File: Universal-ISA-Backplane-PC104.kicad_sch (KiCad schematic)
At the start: 2 parts, among them J201 PC104, J202 PC104_16

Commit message: Initial steps for PCB layout
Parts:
- P201: renamed from J202; value PC104_16 -> (none); footprint Connector_PinSocket_2.54mm:PinSocket_2x20_P2.54mm_Vertical -> (none); symbol Connector_Generic:Conn_02x20_Row_Letter_First -> Universal-ISA-Backplane-symbols:PC104-Platform
- P201: renamed from J201; value PC104 -> (none); footprint Universal-ISA-Backplane:PC104_Platform -> (none); symbol Connector_Generic:Conn_02x32_Row_Letter_First -> Universal-ISA-Backplane-symbols:PC104-Platform
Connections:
- net +12V: now also P201.B9 (Pin_B9); no longer P201.b9 (Pin_b9)
- net +5V: now also P201.B29 (Pin_B29), P201.B3 (Pin_B3), P201.D16 (Pin_D16); no longer P201.b29 (Pin_b29), P201.b3 (Pin_b3), P201.d16 (Pin_d16)
- net -12V: now also P201.B7 (Pin_B7); no longer P201.b7 (Pin_b7)
- net -5V: now also P201.B5 (Pin_B5); no longer P201.b5 (Pin_b5)
- net AEN: now also P201.A11 (Pin_A11); no longer P201.a11 (Pin_a11)
- net BALE: now also P201.B28 (Pin_B28); no longer P201.b28 (Pin_b28)
- net BCLK: now also P201.B20 (Pin_B20); no longer P201.b20 (Pin_b20)
- net DRQ0: now also P201.D9 (Pin_D9); no longer P201.d9 (Pin_d9)
- net DRQ1: now also P201.B18 (Pin_B18); no longer P201.b18 (Pin_b18)
- net DRQ2: now also P201.B6 (Pin_B6); no longer P201.b6 (Pin_b6)
- net DRQ3: now also P201.B16 (Pin_B16); no longer P201.b16 (Pin_b16)
- net DRQ5: now also P201.D11 (Pin_D11); no longer P201.d11 (Pin_d11)
- net DRQ6: now also P201.D13 (Pin_D13); no longer P201.d13 (Pin_d13)
- net DRQ7: now also P201.D15 (Pin_D15); no longer P201.d15 (Pin_d15)
- net GND: now also P201.A32 (Pin_A32), P201.B1 (Pin_B1), P201.B31 (Pin_B31), P201.B32 (Pin_B32), P201.C0 (Pin_C0), P201.D0 (Pin_D0), P201.D18 (Pin_D18), P201.D19 (Pin_D19); no longer P201.a32 (Pin_a32), P201.b1 (Pin_b1), P201.b31 (Pin_b31), P201.b32 (Pin_b32), P201.c0 (Pin_c0), P201.d0 (Pin_d0), P201.d18 (Pin_d18), P201.d19 (Pin_d19)
- net IOCHRDY: now also P201.A10 (Pin_A10); no longer P201.a10 (Pin_a10)
- net IRQ10: now also P201.D3 (Pin_D3); no longer P201.d3 (Pin_d3)
- net IRQ11: now also P201.D4 (Pin_D4); no longer P201.d4 (Pin_d4)
- net IRQ12: now also P201.D5 (Pin_D5); no longer P201.d5 (Pin_d5)
- net IRQ14: now also P201.D7 (Pin_D7); no longer P201.d7 (Pin_d7)
- net IRQ15: now also P201.D6 (Pin_D6); no longer P201.d6 (Pin_d6)
- net IRQ3: now also P201.B25 (Pin_B25); no longer P201.b25 (Pin_b25)
- net IRQ4: now also P201.B24 (Pin_B24); no longer P201.b24 (Pin_b24)
- net IRQ5: now also P201.B23 (Pin_B23); no longer P201.b23 (Pin_b23)
- net IRQ6: now also P201.B22 (Pin_B22); no longer P201.b22 (Pin_b22)
- net IRQ7: now also P201.B21 (Pin_B21); no longer P201.b21 (Pin_b21)
- net IRQ9: now also P201.B4 (Pin_B4); no longer P201.b4 (Pin_b4)
- net LA17: now also P201.C8 (Pin_C8); no longer P201.c8 (Pin_c8)
- net LA18: now also P201.C7 (Pin_C7); no longer P201.c7 (Pin_c7)
- net LA19: now also P201.C6 (Pin_C6); no longer P201.c6 (Pin_c6)
- net LA20: now also P201.C5 (Pin_C5); no longer P201.c5 (Pin_c5)
- net LA21: now also P201.C4 (Pin_C4); no longer P201.c4 (Pin_c4)
- net LA22: now also P201.C3 (Pin_C3); no longer P201.c3 (Pin_c3)
- net LA23: now also P201.C2 (Pin_C2); no longer P201.c2 (Pin_c2)
- net OSC: now also P201.B30 (Pin_B30); no longer P201.b30 (Pin_b30)
- net RESET: now also P201.B2 (Pin_B2); no longer P201.b2 (Pin_b2)
- net SA0: now also P201.A31 (Pin_A31); no longer P201.a31 (Pin_a31)
- net SA1: now also P201.A30 (Pin_A30); no longer P201.a30 (Pin_a30)
- net SA10: now also P201.A21 (Pin_A21); no longer P201.a21 (Pin_a21)
- net SA11: now also P201.A20 (Pin_A20); no longer P201.a20 (Pin_a20)
- net SA12: now also P201.A19 (Pin_A19); no longer P201.a19 (Pin_a19)
- net SA13: now also P201.A18 (Pin_A18); no longer P201.a18 (Pin_a18)
- net SA14: now also P201.A17 (Pin_A17); no longer P201.a17 (Pin_a17)
- net SA15: now also P201.A16 (Pin_A16); no longer P201.a16 (Pin_a16)
- net SA16: now also P201.A15 (Pin_A15); no longer P201.a15 (Pin_a15)
- net SA17: now also P201.A14 (Pin_A14); no longer P201.a14 (Pin_a14)
- net SA18: now also P201.A13 (Pin_A13); no longer P201.a13 (Pin_a13)
- net SA19: now also P201.A12 (Pin_A12); no longer P201.a12 (Pin_a12)
- net SA2: now also P201.A29 (Pin_A29); no longer P201.a29 (Pin_a29)
- net SA3: now also P201.A28 (Pin_A28); no longer P201.a28 (Pin_a28)
- net SA4: now also P201.A27 (Pin_A27); no longer P201.a27 (Pin_a27)
- net SA5: now also P201.A26 (Pin_A26); no longer P201.a26 (Pin_a26)
- net SA6: now also P201.A25 (Pin_A25); no longer P201.a25 (Pin_a25)
- net SA7: now also P201.A24 (Pin_A24); no longer P201.a24 (Pin_a24)
- net SA8: now also P201.A23 (Pin_A23); no longer P201.a23 (Pin_a23)
- net SA9: now also P201.A22 (Pin_A22); no longer P201.a22 (Pin_a22)
- net SD0: now also P201.A9 (Pin_A9); no longer P201.a9 (Pin_a9)
- net SD1: now also P201.A8 (Pin_A8); no longer P201.a8 (Pin_a8)
- net SD10: now also P201.C13 (Pin_C13); no longer P201.c13 (Pin_c13)
- net SD11: now also P201.C14 (Pin_C14); no longer P201.c14 (Pin_c14)
- net SD12: now also P201.C15 (Pin_C15); no longer P201.c15 (Pin_c15)
- net SD13: now also P201.C16 (Pin_C16); no longer P201.c16 (Pin_c16)
- net SD14: now also P201.C17 (Pin_C17); no longer P201.c17 (Pin_c17)
- net SD15: now also P201.C18 (Pin_C18); no longer P201.c18 (Pin_c18)
- net SD2: now also P201.A7 (Pin_A7); no longer P201.a7 (Pin_a7)
- net SD3: now also P201.A6 (Pin_A6); no longer P201.a6 (Pin_a6)
- net SD4: now also P201.A5 (Pin_A5); no longer P201.a5 (Pin_a5)
- net SD5: now also P201.A4 (Pin_A4); no longer P201.a4 (Pin_a4)
- net SD6: now also P201.A3 (Pin_A3); no longer P201.a3 (Pin_a3)
- net SD7: now also P201.A2 (Pin_A2); no longer P201.a2 (Pin_a2)
- net SD8: now also P201.C11 (Pin_C11); no longer P201.c11 (Pin_c11)
- net SD9: now also P201.C12 (Pin_C12); no longer P201.c12 (Pin_c12)
- net TC: now also P201.B27 (Pin_B27); no longer P201.b27 (Pin_b27)
- net ~{DACK0}: now also P201.D8 (Pin_D8); no longer P201.d8 (Pin_d8)
- net ~{DACK1}: now also P201.B17 (Pin_B17); no longer P201.b17 (Pin_b17)
- net ~{DACK2}: now also P201.B26 (Pin_B26); no longer P201.b26 (Pin_b26)
- net ~{DACK3}: now also P201.B15 (Pin_B15); no longer P201.b15 (Pin_b15)
- net ~{DACK5}: now also P201.D10 (Pin_D10); no longer P201.d10 (Pin_d10)
- net ~{DACK6}: now also P201.D12 (Pin_D12); no longer P201.d12 (Pin_d12)
- net ~{DACK7}: now also P201.D14 (Pin_D14); no longer P201.d14 (Pin_d14)
- net ~{IOCHK}: now also P201.A1 (Pin_A1); no longer P201.a1 (Pin_a1)
- net ~{IOCS16}: now also P201.D2 (Pin_D2); no longer P201.d2 (Pin_d2)
- net ~{IOR}: now also P201.B14 (Pin_B14); no longer P201.b14 (Pin_b14)
- net ~{IOW}: now also P201.B13 (Pin_B13); no longer P201.b13 (Pin_b13)
- net ~{MASTER}: now also P201.D17 (Pin_D17); no longer P201.d17 (Pin_d17)
- net ~{MEMCS16}: now also P201.D1 (Pin_D1); no longer P201.d1 (Pin_d1)
- net ~{MEMR}: now also P201.C9 (Pin_C9); no longer P201.c9 (Pin_c9)
- net ~{MEMW}: now also P201.C10 (Pin_C10); no longer P201.c10 (Pin_c10)
- net ~{REFRESH}: now also P201.B19 (Pin_B19); no longer P201.b19 (Pin_b19)
- net ~{SBHE}: now also P201.C1 (Pin_C1); no longer P201.c1 (Pin_c1)
- net ~{SMEMR}: now also P201.B12 (Pin_B12); no longer P201.b12 (Pin_b12)
- net ~{SMEMW}: now also P201.B11 (Pin_B11); no longer P201.b11 (Pin_b11)
- net ~{SRDY}: now also P201.B8 (Pin_B8); no longer P201.b8 (Pin_b8)

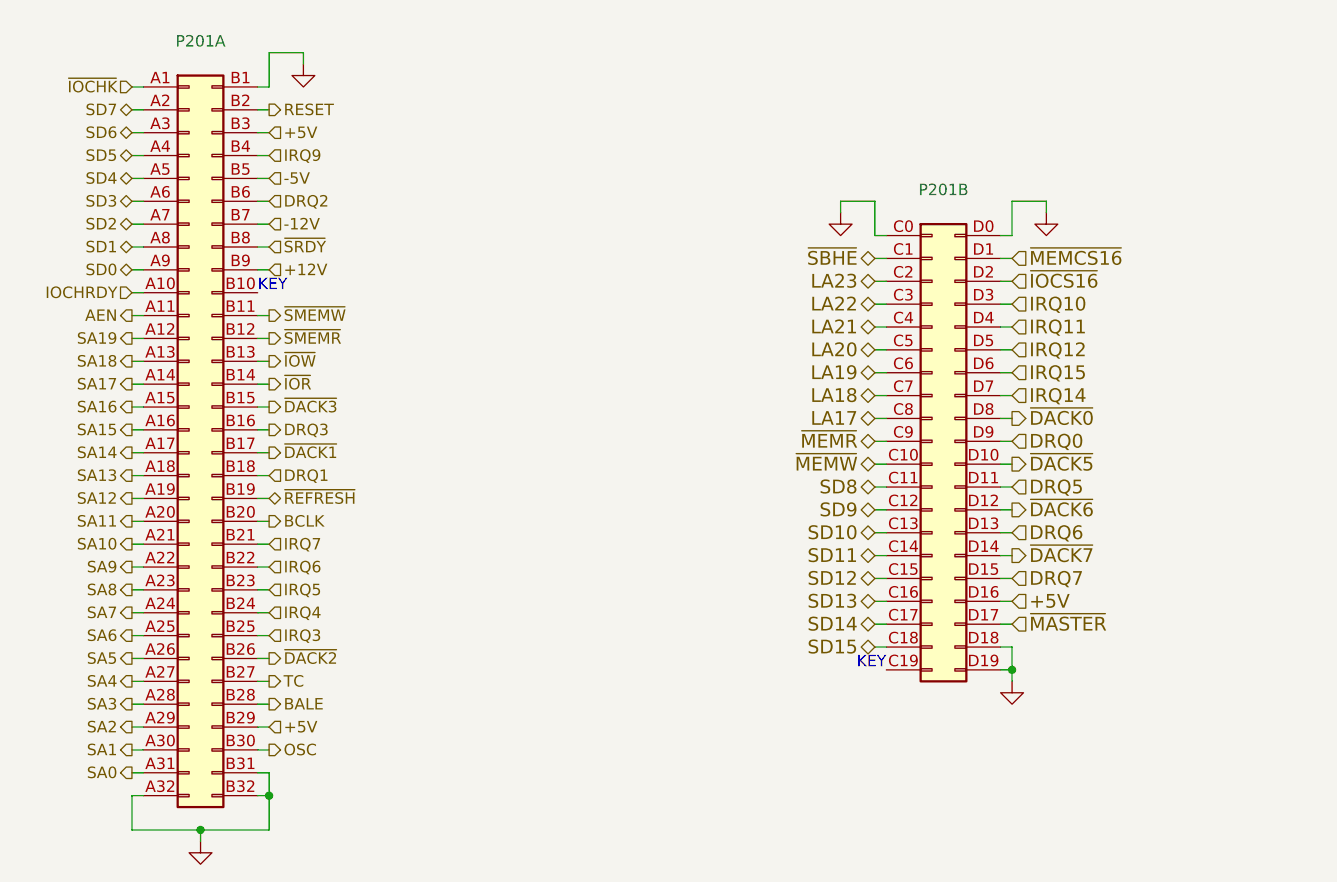
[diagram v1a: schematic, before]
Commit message: PC/104 and ISA connector fixes
And further development
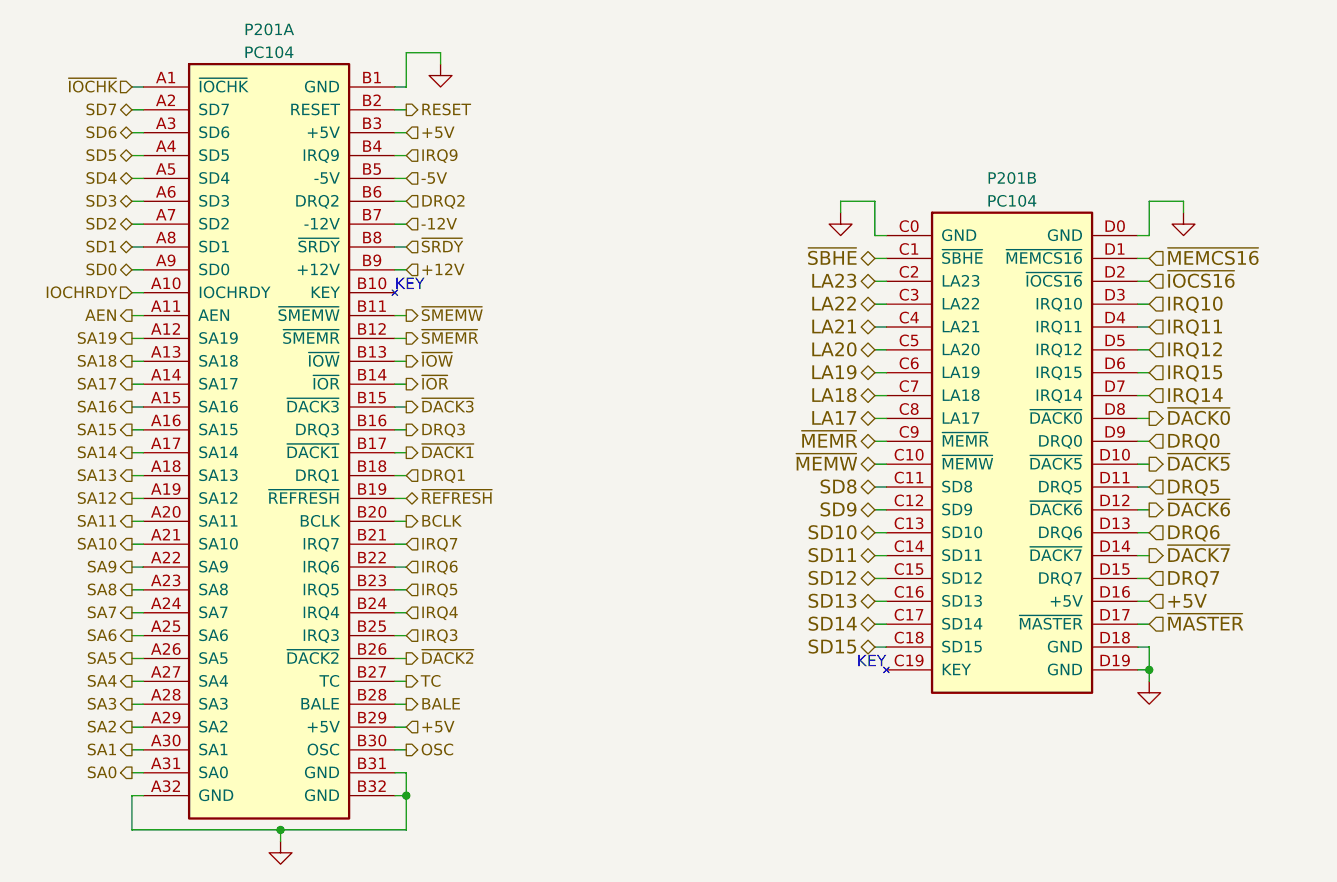
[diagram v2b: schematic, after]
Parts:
- P201: value (none) -> PC104; footprint (none) -> Universal-ISA-Backplane:PC104_Platform
